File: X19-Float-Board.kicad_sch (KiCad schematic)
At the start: 0 parts

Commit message: Draft of Schematic
I just pasted in my old draft so it's on the repository
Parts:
- added BT1, BT2: 9V, symbol Device:Battery
- added C1, C5: 10nF, symbol Device:C_Small
- added C2, C3, C8: 100nF, symbol Device:C_Small
- added C4: 4.7µF, symbol Device:C_Small
- added C6: .1µF, symbol Device:C_Small
- added C7: 5.6nF, symbol Device:C_Small
- added C9: 44µF, symbol Device:C_Small
- added D1: D_Schottky, symbol Device:D_Schottky
- added F1: 2A 12V PTC fuse, symbol Device:Fuse
- added J1: Motor, symbol Connector:Conn_01x02_Pin
- added L1: 4.7µH, symbol Device:L_Small
- added Q1: NMOS, symbol Simulation_SPICE:NMOS
- added R1, R2, R4, R6, R7: 10kΩ, symbol Device:R_Small_US
- added R10, R9: 4.7kΩ, symbol Device:R_Small_US
- added R3: 25kΩ, symbol Device:R_Small_US
- added R5: 100kΩ, symbol Device:R_Small_US
- added R8: 100Ω, symbol Device:R_Small_US
- added SW1: SW_Push, symbol Switch:SW_Push
- added SW2: SW_Nidec_CAS-120A1, Button_Switch_SMD:Nidec_Copal_CAS-120A, symbol Switch:SW_Nidec_CAS-120A1
- added U1: STM32F030F4Px, Package_SO:TSSOP-20_4.4x6.5mm_P0.65mm, symbol MCU_ST_STM32F0:STM32F030F4Px
- added U2: AMS1117-3.3, Package_TO_SOT_SMD:SOT-223-3_TabPin2, symbol Regulator_Linear:AMS1117-3.3
- added U3: RFM95W-868S2, symbol RF_Module:RFM95W-868S2
- added U4: TPS54336ADDA, Package_SO:TI_SO-PowerPAD-8_ThermalVias, symbol Regulator_Switching:TPS54336ADDA
- added U5: MS5837-xxBA, Sensor_Pressure:TE_MS5837-xxBA, symbol Sensor_Pressure:MS5837-xxBA
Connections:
- new net: C2.1, R2.2, SW1.2, U1.4 (NRST)
- new net: C8.1, U4.1 (BOOT)
- new net: C8.2, L1.1, U4.3 (PH)
- new net: R4.2, R5.1, U4.5 (VSENSE)
- new net: C6.1, C7.1, U4.6 (COMP)
- new net: C5.1, U4.8 (SS)
- new net: D1.2 (A), J1.1 (Pin_1), Q1.1 (D)
- new net: R7.2, R8.1, U1.20 (PA14)
- new net: R1.2, U1.1 (BOOT0)
- new net: C7.2, R3.1
- new net: BT1.1 (+), BT2.1 (+), F1.2
- new net 12V: D1.1 (K), J1.2 (Pin_2)
- new net 3.3: U2.2 (VO)
- new net 3.3V: C3.1, C4.1, R10.2, R2.1, R6.2, R9.1, U1.16 (VDD), U1.5 (VDDA), U3.13 (3.3V), U5.2 (VDD)
- new net 5V: C9.2, L1.2, R5.2, U2.3 (VI)
- new net 9V: C1.2, F1.1, U4.2 (VIN)
- new net Depth_SCL: R10.1, U1.17 (PA9), U5.3 (SCL)
- new net Depth_SDA: R9.2, U1.18 (PA10), U5.4 (SDA)
- new net GND: BT1.2 (-), BT2.2 (-), C1.1, C2.2, C3.2, C4.2, C5.2, C6.2, C9.1, Q1.3 (S), R1.1, R3.2, R4.1, R7.1, SW1.1, SW2.2 (B), U1.15 (VSS), U2.1 (GND), U3.1 (GND), U3.10 (GND), U3.8 (GND), U4.4 (GND), U5.1 (GND)
- new net motor_ctrl: Q1.2 (G), R8.2
- new net rf_int: U1.7 (PA1), U3.14 (DIO0)
- new net rf_miso: U1.12 (PA6), U3.2 (MISO)
- new net rf_mosi: U1.13 (PA7), U3.3 (MOSI)
- new net rf_nss: U1.9 (PA3), U3.5 (NSS)
- new net rf_reset: U1.8 (PA2), U3.6 (RESET)
- new net rf_sck: U1.11 (PA5), U3.4 (SCK)
- new net switch: R6.1, SW2.1 (C), U1.6 (PA0)

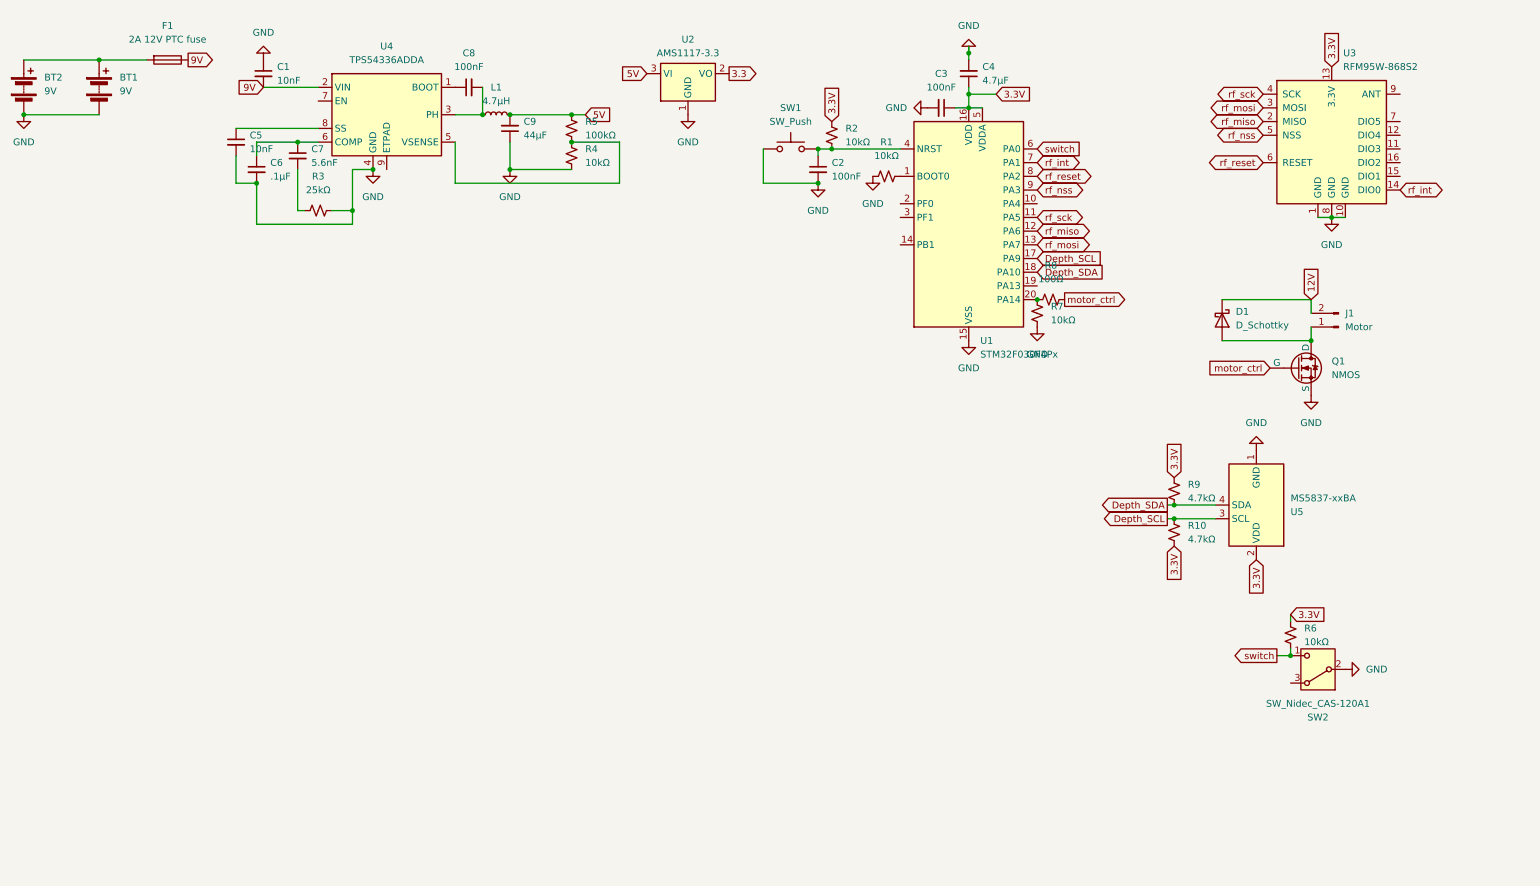
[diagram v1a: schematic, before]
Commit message: Added hierarchical sheets
Added the sheets and how I'm splitting up the components, may have used too many, I'm not sure how to use these. Will update components and wiring soon
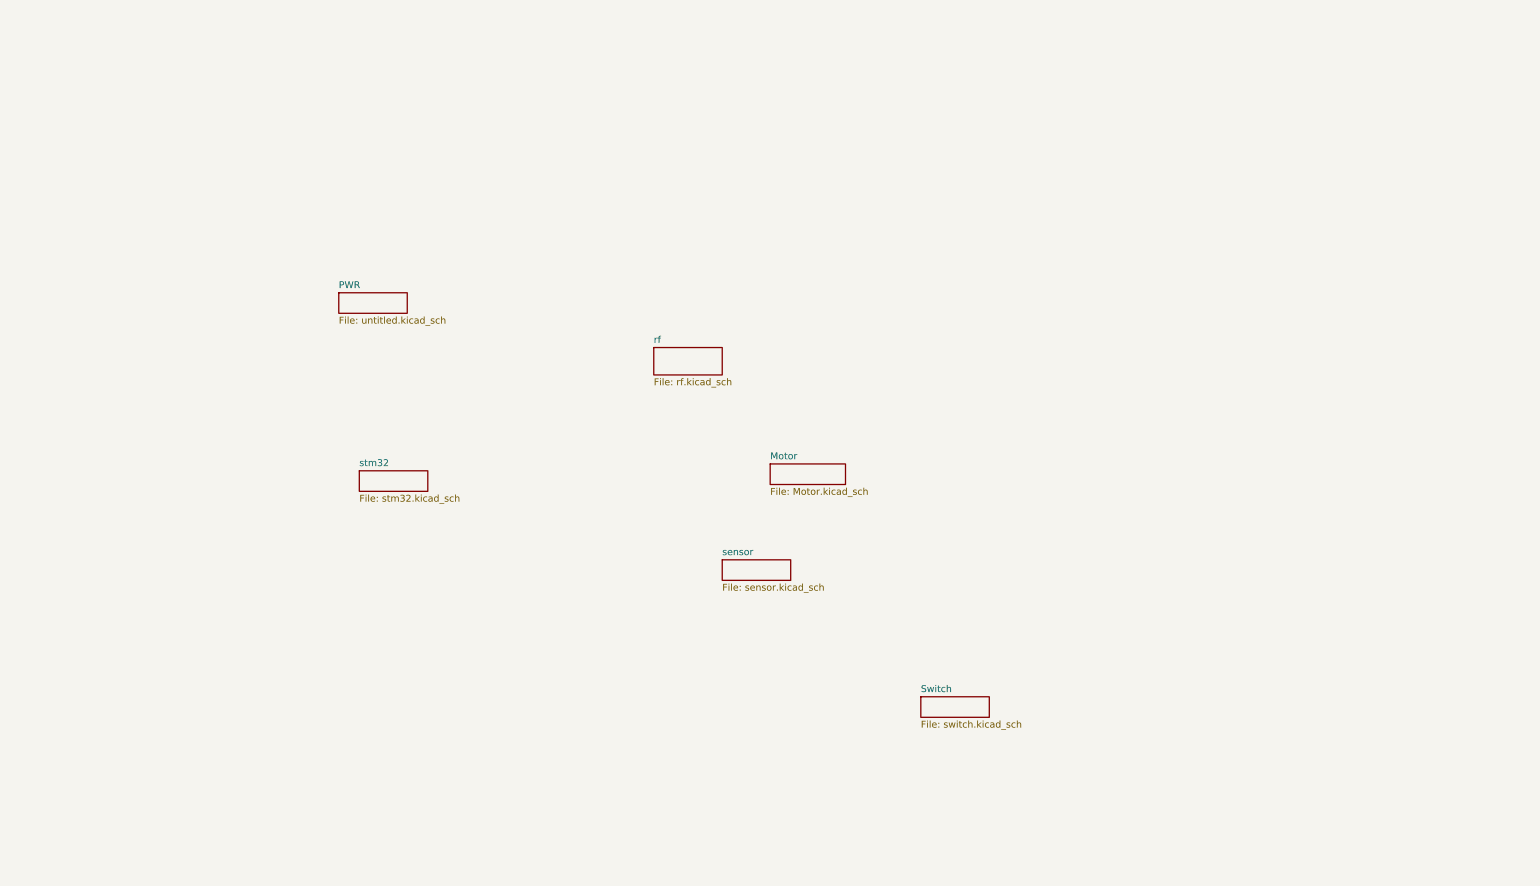
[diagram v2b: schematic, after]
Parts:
- removed BT1, BT2: 9V, symbol Device:Battery
- removed C1, C5: 10nF, symbol Device:C_Small
- removed C2, C3, C8: 100nF, symbol Device:C_Small
- removed C4: 4.7µF, symbol Device:C_Small
- removed C6: .1µF, symbol Device:C_Small
- removed C7: 5.6nF, symbol Device:C_Small
- removed C9: 44µF, symbol Device:C_Small
- removed D1: D_Schottky, symbol Device:D_Schottky
- removed F1: 2A 12V PTC fuse, symbol Device:Fuse
- removed J1: Motor, symbol Connector:Conn_01x02_Pin
- removed L1: 4.7µH, symbol Device:L_Small
- removed Q1: NMOS, symbol Simulation_SPICE:NMOS
- removed R1, R2, R4, R6, R7: 10kΩ, symbol Device:R_Small_US
- removed R10, R9: 4.7kΩ, symbol Device:R_Small_US
- removed R3: 25kΩ, symbol Device:R_Small_US
- removed R5: 100kΩ, symbol Device:R_Small_US
- removed R8: 100Ω, symbol Device:R_Small_US
- removed SW1: SW_Push, symbol Switch:SW_Push
- removed SW2: SW_Nidec_CAS-120A1, Button_Switch_SMD:Nidec_Copal_CAS-120A, symbol Switch:SW_Nidec_CAS-120A1
- removed U1: STM32F030F4Px, Package_SO:TSSOP-20_4.4x6.5mm_P0.65mm, symbol MCU_ST_STM32F0:STM32F030F4Px
- removed U2: AMS1117-3.3, Package_TO_SOT_SMD:SOT-223-3_TabPin2, symbol Regulator_Linear:AMS1117-3.3
- removed U3: RFM95W-868S2, symbol RF_Module:RFM95W-868S2
- removed U4: TPS54336ADDA, Package_SO:TI_SO-PowerPAD-8_ThermalVias, symbol Regulator_Switching:TPS54336ADDA
- removed U5: MS5837-xxBA, Sensor_Pressure:TE_MS5837-xxBA, symbol Sensor_Pressure:MS5837-xxBA
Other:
- added sheet Motor (Motor.kicad_sch)
- added sheet PWR (untitled.kicad_sch)
- added sheet Switch (switch.kicad_sch)
- added sheet rf (rf.kicad_sch)
- added sheet sensor (sensor.kicad_sch)
- added sheet stm32 (stm32.kicad_sch)

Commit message: Overhaul
Overhauled the schematic so all the components are correct, rewired power to be 12 V instead of 9 V and connected hierarchical labels between modules. Added more decoupling capacitors where they were missing.
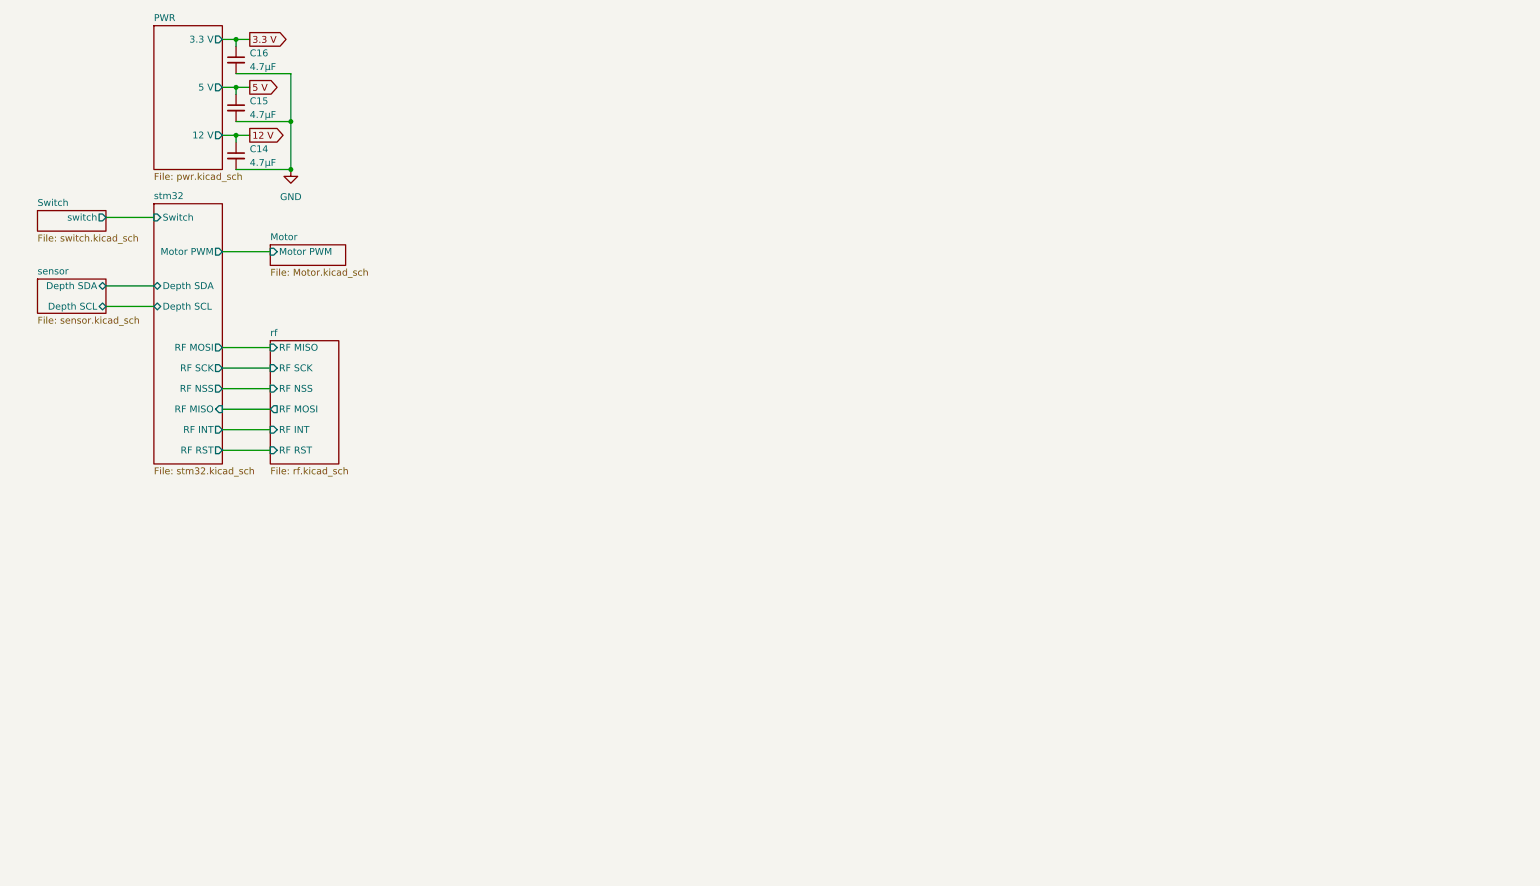
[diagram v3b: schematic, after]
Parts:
- added C14, C15, C16: 4.7µF, symbol Device:C_Small
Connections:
- new net 12 V: C14.1
- new net 3.3 V: C16.1
- new net 5 V: C15.1
- new net GND: C14.2, C15.2, C16.2
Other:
- sheet Motor ports: added Motor PWM; removed none
- sheet PWR: file untitled.kicad_sch -> pwr.kicad_sch
- sheet PWR ports: added 12 V, 3.3 V, 5 V; removed none
- sheet Switch ports: added switch; removed none
- sheet rf ports: added RF INT, RF MISO, RF MOSI, RF NSS, RF RST, RF SCK; removed none
- sheet sensor ports: added Depth SCL, Depth SDA; removed none
- sheet stm32 ports: added Depth SCL, Depth SDA, Motor PWM, RF INT, RF MISO, RF MOSI, RF NSS, RF RST, RF SCK, Switch; removed none

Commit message: Gave footprints to everything
Footprints
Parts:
- C14, C15, C16: footprint (none) -> Capacitor_SMD:C_0603_1608Metric
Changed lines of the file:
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@@
 			)
 		)
-		(property "Footprint" ""
+		(property "Footprint" "Capacitor_SMD:C_0603_1608Metric"
 			(at 54.61 31.75 0)
 			(hide yes)
@@
 			)
 		)
-		(property "Footprint" ""
+		(property "Footprint" "Capacitor_SMD:C_0603_1608Metric"
 			(at 54.61 22.86 0)
 			(hide yes)
@@
 			)
 		)
-		(property "Footprint" ""
+		(property "Footprint" "Capacitor_SMD:C_0603_1608Metric"
 			(at 54.61 40.64 0)
 			(hide yes)

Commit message: Modifications to power system to support what is required
modified
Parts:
- removed C15: 4.7µF, Capacitor_SMD:C_0603_1608Metric, symbol Device:C_Small
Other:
- sheet PWR ports: added none; removed 5 V
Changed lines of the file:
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@@
-	)
-	(junction
-		(at 64.77 34.29)
-		(diameter 0)
-		(color 0 0 0 0)
 	)
 	(junction
@@
 		(color 0 0 0 0)
 	)
-	(junction
-		(at 54.61 27.94)
-		(diameter 0)
-		(color 0 0 0 0)
-	)
 	(wire
 		(pts
@@
 	(wire
 		(pts
-			(xy 52.07 27.94) (xy 54.61 27.94)
-		)
-		(stroke
-			(width 0)
-			(type default)
-		)
-	)
-	(wire
-		(pts
 			(xy 54.61 19.05) (xy 57.15 19.05)
 		)
@@
 	(wire
 		(pts
-			(xy 54.61 34.29) (xy 64.77 34.29)
-		)
-		(stroke
-			(width 0)
-			(type default)
-		)
-	)
-	(wire
-		(pts
 			(xy 52.07 80.01) (xy 60.96 80.01)
 		)
@@
 	(wire
 		(pts
-			(xy 64.77 34.29) (xy 64.77 43.18)
-		)
-		(stroke
-			(width 0)
-			(type default)
-		)
-	)
-	(wire
-		(pts
 			(xy 52.07 91.44) (xy 60.96 91.44)
 		)
@@
 	(wire
 		(pts
-			(xy 54.61 27.94) (xy 54.61 29.21)
-		)
-		(stroke
-			(width 0)
-			(type default)
-		)
-	)
-	(wire
-		(pts
 			(xy 30.48 64.77) (xy 39.37 64.77)
 		)
@@
 	(wire
 		(pts
-			(xy 54.61 27.94) (xy 57.15 27.94)
-		)
-		(stroke
-			(width 0)
-			(type default)
-		)
-	)
-	(wire
-		(pts
 			(xy 54.61 43.18) (xy 64.77 43.18)
 		)
@@
 	(wire
 		(pts
-			(xy 64.77 25.4) (xy 64.77 34.29)
+			(xy 64.77 25.4) (xy 64.77 43.18)
 		)
 		(stroke
@@
 		(property "Intersheetrefs" "${INTERSHEET_REFS}"
 			(at 64.6104 36.83 0)
-			(hide yes)
-			(show_name no)
-			(do_not_autoplace no)
-			(effects
-				(font
-					(size 1.27 1.27)
-				)
-				(justify left)
-			)
-		)
-	)
-	(global_label "5 V"
-		(shape output)
-		(at 57.15 27.94 0)
-		(fields_autoplaced yes)
-		(effects
-			(font
-				(size 1.27 1.27)
-			)
-			(justify left)
-		)
-		(property "Intersheetrefs" "${INTERSHEET_REFS}"
-			(at 63.4009 27.94 0)
 			(hide yes)
 			(show_name no)
@@
 	(symbol
 		(lib_id "Device:C_Small")
-		(at 54.61 31.75 0)
-		(unit 1)
-		(body_style 1)
-		(exclude_from_sim no)
-		(in_bom yes)
-		(on_board yes)
-		(in_pos_files yes)
-		(dnp no)
-		(fields_autoplaced yes)
-		(property "Reference" "C15"
-			(at 57.15 30.4862 0)
-			(show_name no)
-			(do_not_autoplace no)
-			(effects
-				(font
-					(size 1.27 1.27)
-				)
-				(justify left)
-			)
-		)
-		(property "Value" "4.7µF"
-			(at 57.15 33.0262 0)
-			(show_name no)
-			(do_not_autoplace no)
-			(effects
-				(font
-					(size 1.27 1.27)
-				)
-				(justify left)
-			)
-		)
-		(property "Footprint" "Capacitor_SMD:C_0603_1608Metric"
-			(at 54.61 31.75 0)
-			(hide yes)
-			(show_name no)
-			(do_not_autoplace no)
-			(effects
-				(font
-					(size 1.27 1.27)
-				)
-			)
-		)
-		(property "Datasheet" ""
-			(at 54.61 31.75 0)
-			(hide yes)
-			(show_name no)
-			(do_not_autoplace no)
-			(effects
-				(font
-					(size 1.27 1.27)
-				)
-			)
-		)
-		(property "Description" "Unpolarized capacitor, small symbol"
-			(at 54.61 31.75 0)
-			(hide yes)
-			(show_name no)
-			(do_not_autoplace no)
-			(effects
-				(font
-					(size 1.27 1.27)
-				)
-			)
-		)
-		(pin "1"
-		)
-		(pin "2"
-		)
-		(instances
-			(project "X19-Float-Board"
-				(path "/00000000-0000-0000-0000-000060e6118b"
-					(reference "C15")
-					(unit 1)
-				)
-			)
-		)
-	)
-	(symbol
-		(lib_id "Device:C_Small")
 		(at 54.61 22.86 0)
 		(unit 1)
@@
 			(effects
 				(font
-					(size 1.27 1.27)
-				)
-				(justify right)
-			)
-		)
-		(pin "5 V" output
-			(at 52.07 27.94 0)
-			(effects
-				(font

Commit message: USB-C + Complete wiring
Compltetly wired the pcb (I don't understand the DRC errors) and added a usb C to flash the stm, modified the switch to be the BOOT0 for the stm so it controls whether the stm is in flash mode
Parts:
- renumbered C14 to C_D_PWR_12, C16 to C_D_PWR_3.3
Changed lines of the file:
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@@
 		(dnp no)
 		(fields_autoplaced yes)
-		(property "Reference" "C16"
+		(property "Reference" "C_D_PWR_3.3"
 			(at 57.15 21.5962 0)
 			(show_name no)
@@
 			(project "X19-Float-Board"
 				(path "/00000000-0000-0000-0000-000060e6118b"
-					(reference "C16")
+					(reference "C_D_PWR_3.3")
 					(unit 1)
 				)
@@
 		(dnp no)
 		(fields_autoplaced yes)
-		(property "Reference" "C14"
+		(property "Reference" "C_D_PWR_12"
 			(at 57.15 39.3762 0)
 			(show_name no)
@@
 			(project "X19-Float-Board"
 				(path "/00000000-0000-0000-0000-000060e6118b"
-					(reference "C14")
+					(reference "C_D_PWR_12")
 					(unit 1)
 				)

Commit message: Update
Update
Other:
- sheet sensor renamed Sensors
- added sheet TELEM (TELEM.kicad_sch)
- added sheet USB-C (USB-C.kicad_sch)
- note added: "TODO: add new components, add more decoupling near every power, 4 layer, find where to put temperature sensor Clean up dense scematic in sensors"
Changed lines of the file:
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@@
 		(company "Purdue ROV")
+	)
+	(text "TODO: add new components, add more decoupling near every power, 4 layer, find where to put temperature sensor\nClean up dense scematic in sensors\n"
+		(exclude_from_sim no)
+		(at 220.726 67.056 0)
+		(effects
+			(font
+				(size 1.27 1.27)
+			)
+		)
 	)
 	(junction
@@
 	)
 	(sheet
+		(at 81.28 115.57)
+		(size 12.7 55.88)
+		(exclude_from_sim no)
+		(in_bom yes)
+		(on_board yes)
+		(dnp no)
+		(fields_autoplaced yes)
+		(stroke
+			(width 0.1524)
+			(type solid)
+		)
+		(fill
+			(color 0 0 0 0)
+		)
+		(property "Sheetname" "TELEM"
+			(at 81.28 114.8584 0)
+			(show_name no)
+			(do_not_autoplace no)
+			(effects
+				(font
+					(size 1.27 1.27)
+				)
+				(justify left bottom)
+			)
+		)
+		(property "Sheetfile" "TELEM.kicad_sch"
+			(at 81.28 172.0346 0)
+			(show_name no)
+			(do_not_autoplace no)
+			(effects
+				(font
+					(size 1.27 1.27)
+				)
+				(justify left top)
+			)
+		)
+		(pin "PWR_ALERT" output
+			(at 81.28 119.38 180)
+			(effects
+				(font
+					(size 1.27 1.27)
+				)
+				(justify left)
+			)
+		)
+		(pin "PWR_SCL" output
+			(at 81.28 124.46 180)
+			(effects
+				(font
+					(size 1.27 1.27)
+				)
+				(justify left)
+			)
+		)
+		(pin "PWR_SDA" output
+			(at 81.28 132.08 180)
+			(effects
+				(font
+					(size 1.27 1.27)
+				)
+				(justify left)
+			)
+		)
+		(pin "TMP_ALERT" output
+			(at 81.28 139.7 180)
+			(effects
+				(font
+					(size 1.27 1.27)
+				)
+				(justify left)
+			)
+		)
+		(pin "TMP_SCL" output
+			(at 81.28 149.86 180)
+			(effects
+				(font
+					(size 1.27 1.27)
+				)
+				(justify left)
+			)
+		)
+		(pin "TMP_SDA" output
+			(at 81.28 160.02 180)
+			(effects
+				(font
+					(size 1.27 1.27)
+				)
+				(justify left)
+			)
+		)
+		(instances
+			(project "X19-Float-Board"
+				(path "/00000000-0000-0000-0000-000060e6118b"
+					(page "9")
+				)
+			)
+		)
+	)
+	(sheet
 		(at 17.78 63.5)
 		(size 12.7 6.35)
@@
 			(color 0 0 0 0)
 		)
-		(property "Sheetname" "sensor"
+		(property "Sheetname" "Sensors"
 			(at 17.78 62.7884 0)
 			(show_name no)
@@
 				)
 			)
+		)
+	)
+	(sheet
+		(at 39.37 105.41)
+		(size 12.7 26.67)
+		(exclude_from_sim no)
+		(in_bom yes)
+		(on_board yes)
+		(dnp no)
+		(fields_autoplaced yes)
+		(stroke
+			(width 0.1524)
+			(type solid)
+		)
+		(fill
+			(color 0 0 0 0)
+		)
+		(property "Sheetname" "USB-C"
+			(at 39.37 104.6984 0)
+			(show_name no)
+			(do_not_autoplace no)
+			(effects
+				(font
+					(size 1.27 1.27)
+				)
+				(justify left bottom)
+			)
+		)
+		(property "Sheetfile" "USB-C.kicad_sch"
+			(at 39.37 132.6646 0)
+			(show_name no)
+			(do_not_autoplace no)
+			(effects
+				(font
+					(size 1.27 1.27)
+				)
+				(justify left top)
+			)
+		)
+		(pin "USB-C_DN2" input
+			(at 39.37 107.95 180)
+			(effects
+				(font
+					(size 1.27 1.27)
+				)
+				(justify left)
+			)
+		)
+		(pin "USB-C_DP2" input
+			(at 39.37 111.76 180)
+			(effects
+				(font
+					(size 1.27 1.27)
+				)
+				(justify left)
+			)
+		)
+		(pin "USB-C_VBUS_A" input
+			(at 39.37 114.3 180)
+			(effects
+				(font
+					(size 1.27 1.27)
+				)
+				(justify left)
+			)
+		)
+		(instances
+			(project "X19-Float-Board"
+				(path "/00000000-0000-0000-0000-000060e6118b"
+					(page "8")
+				)
+			)

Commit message: Small changes to hierarchy
Small Changes
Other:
- sheet Sensors ports: added LIGHT VOLTAGE; removed none
